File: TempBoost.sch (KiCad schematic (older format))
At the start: 63 parts, among them J1 Conn_01x02, J2 Conn_01x02, Q201 Q_NMOS_GSD, SW101 SW_SPST, T101 3FD-224, U101 DF005S2, U201 MIC2920, U203 UCC27517A, U204 2925, U205 LM2904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

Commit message: Base Placement
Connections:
- net labels removed: VRECT-
- wire segments 165 -> 166
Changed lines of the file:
@@
 Text GLabel 870  5400 0    39   Input ~ 0
 VRECT+
-Text GLabel 875  5795 0    39   Input ~ 0
-VRECT-
 Text Notes 1285 5015 0    39   ~ 0
 12V Supply
@@
 Text GLabel 5100 5300 2    39   Input ~ 0
 Gate
-Text GLabel 3250 5800 0    39   Input ~ 0
-VRECT-
 Text GLabel 3250 5500 0    39   Input ~ 0
 VPWM
@@
 Text Label 3450 6800 0    39   ~ 0
 Ref_in
+$Comp
+L GND #PWR025
+U 1 1 5CAE3F10
+P 3250 5800
+F 0 "#PWR025" H 3250 5550 50  0001 C CNN
+F 1 "GND" H 3250 5650 50  0000 C CNN
+F 2 "" H 3250 5800 50  0001 C CNN
+F 3 "" H 3250 5800 50  0001 C CNN
+	1    3250 5800
+	0    1    -1   0
+$EndComp
+$Comp
+L GND #PWR026
+U 1 1 5CAE4C64
+P 1150 5900
+F 0 "#PWR026" H 1150 5650 50  0001 C CNN
+F 1 "GND" H 1150 5750 50  0000 C CNN
+F 2 "" H 1150 5900 50  0001 C CNN
+F 3 "" H 1150 5900 50  0001 C CNN
+	1    1150 5900
+	1    0    0    -1
+$EndComp
+Wire Wire Line
+	1150 5900 1150 5800
+Text Label 2100 4400 0    39   ~ 0
+GND
 $EndSCHEMATC

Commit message: Starting Layout
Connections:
- wire segments 166 -> 230

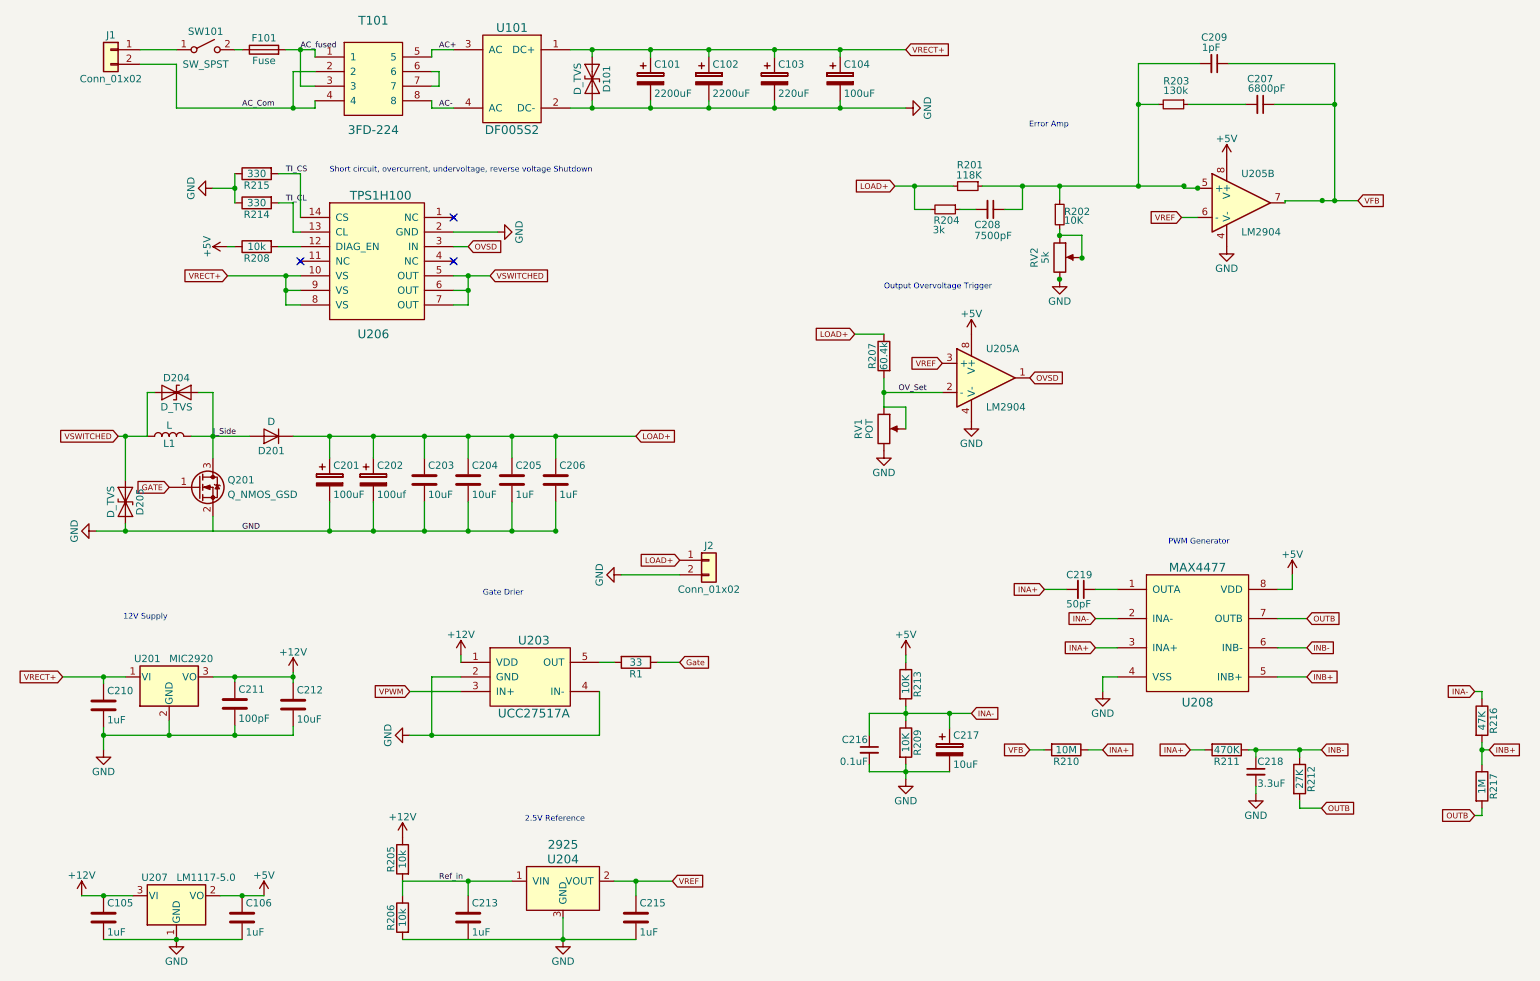
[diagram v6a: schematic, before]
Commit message: More Routing
PWM Generator is routed so that it now works but the freqency is 70Hz rather than 70k. RIP
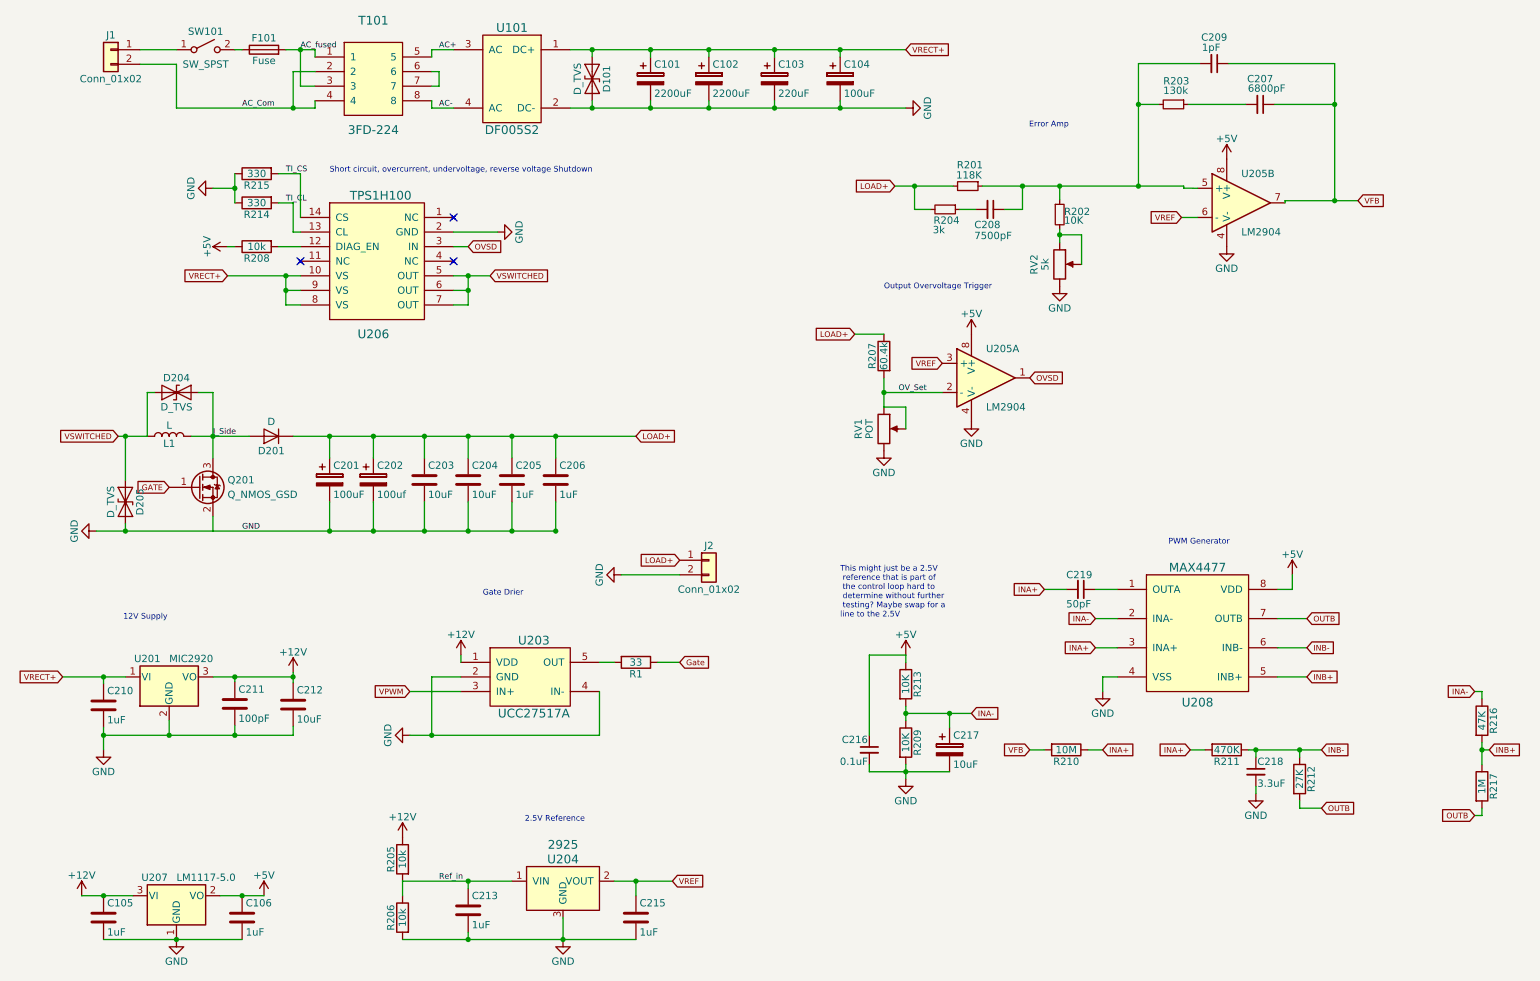
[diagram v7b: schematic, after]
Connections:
- wire segments 230 -> 169
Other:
- note added: "This might just be a 2.5V\n reference that is part of\n the control loop hard to\n determine without further\n testing? Maybe swap for a\nline to the 2.5V\n"
- moved on the sheet: C213, RV2

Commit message: Done
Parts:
- removed C216: 0.1uF, Capacitors_THT:C_Axial_L5.1mm_D3.1mm_P10.00mm_Horizontal, symbol C_Small
- removed C217: 10uF, Capacitors_THT:C_Disc_D5.0mm_W2.5mm_P2.50mm, symbol CP
- removed R209, R213: 10K, Resistors_SMD:R_0805, symbol R
- added TP1, TP2, TP3: TEST, Connectors:1pin, symbol TEST
- C218: value 3.3uF -> 22nF
- R211: value 470K -> 47K
- R212: value 27K -> 5K
- R216: value 47K -> 4.7K
- R217: value 1M -> 500k
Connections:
- net VPWM is gone; now on net OUTB: U203.3 (IN+)
- net GND: now also Q201.2 (S)
- net Gate: now also TP3.1
- net INA-: no longer U208.2 (INA-)
- net OUTB: now also TP1.1
- net VFB: now also TP2.1
- net VREF: now also U208.2 (INA-)
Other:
- note removed: "This might just be a 2.5V\n reference that is part of\n the control loop hard to\n determine without further\n testing? Maybe swap for a\nline to the 2.5V\n"
- moved on the sheet: C218, R210, R211, R212
